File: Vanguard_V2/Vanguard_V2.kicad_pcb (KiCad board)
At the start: 4 copper layers, 55.9 x 30.5 mm, 75 parts, among them IC1 ST1L05CPU33R, IC2 MAX-M10S-00B, IC3 ADXL375BCCZ-RL, IC4 ASM330LHHTR, J1 Conn_01x02_Pin, J2 Conn_01x05_Pin, J3 MEM2067-02-180-00-A, J4 Conn_01x04_Pin, J5 Conn_01x02_Pin, J6 Conn_01x02_Pin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

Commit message: V2 Board Ready
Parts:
- removed R10: 10k, Resistor_SMD:R_0402_1005Metric
- C15, C16, C17, C7, C8, IC1, R3, U2: moved to F.Cu
- C19, C23, C31, C32, D3, FB2, FB3, IC2, J7, R11, R6, R7: moved to B.Cu
- J6: value Conn_01x02_Pin -> Screw_Terminal_01x04; footprint Connector_PinHeader_2.54mm:PinHeader_1x02_P2.54mm_Vertical -> TerminalBlock:TerminalBlock_Xinya_XY308-2.54-4P_1x04_P2.54mm_Horizontal
- moved R7 110.0 mm to (141.4, 85.8), turned to 180 degrees
- moved R6 108.8 mm to (139.8, 85.3), turned to -90 degrees
- moved C11 107.6 mm to (127.0, 78.6), turned to 90 degrees
- moved C10 107.0 mm to (126.0, 78.6), turned to 90 degrees
- moved C9 106.0 mm to (125.0, 78.6), turned to 90 degrees
- moved C12 103.8 mm to (130.0, 78.6), turned to 90 degrees
- moved C13 102.8 mm to (129.0, 78.6), turned to 90 degrees
- moved C19 102.3 mm to (138.2, 85.8), turned to 180 degrees
- moved C14 101.9 mm to (128.0, 78.6), turned to 90 degrees
- moved D1 94.2 mm to (124.4, 101.7), turned to 180 degrees
- moved C26 92.9 mm to (151.9, 91.0)
- moved C25 90.9 mm to (149.6, 91.0), turned to 180 degrees
- moved J5 89.9 mm to (134.9, 74.2), turned to 90 degrees
- moved C24 89.4 mm to (146.8, 95.8), turned to 180 degrees
- moved R5 88.6 mm to (110.3, 100.4), turned to -90 degrees
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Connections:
- C24 pad 1: Net-(IC4-VDDIO) -> +3.3V
- C25 pad 1: Net-(IC4-VDDIO) -> +3.3V
- C26 pad 1: Net-(IC4-VDDIO) -> +3.3V
- IC4 pad 5: Net-(IC4-VDDIO) -> +3.3V
- J6 pad 1: GND -> unconnected-(J6-Pin_1-Pad1)
- J6 pad 2: +3.3V -> unconnected-(J6-Pin_2-Pad2)
- U1 pad 2: unconnected-(U1-PE3-Pad2) -> SERVO_5_PWM
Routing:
- net +3.3V: track 1.46 -> 111.1 mm, vias 0 -> 16
- net I2C1_SCL: track 0.00 -> 99.0 mm, vias 0 -> 6
- net I2C1_SDA: track 0.00 -> 89.0 mm, vias 0 -> 7
- net GND: track 5.82 -> 81.5 mm, vias 2 -> 53
- net BOOT0: track 0.00 -> 40.2 mm, vias 0 -> 2
- net USB_DP: track 0.00 -> 40.1 mm, vias 0 -> 2
- net USB_DM: track 0.00 -> 39.9 mm, vias 0 -> 2
- net RST: track 0.00 -> 30.1 mm
- net SPI1_MOSI: track 0.00 -> 23.4 mm, vias 0 -> 2
- net SERVO_5_PWM: track 0.00 -> 21.1 mm, vias 0 -> 1
- net SPI1_SCK: track 0.00 -> 21.1 mm, vias 0 -> 1
- net Net-(C1-Pad1): track 0.00 -> 18.8 mm, vias 0 -> 2
- net SD_CS: track 0.00 -> 18.5 mm, vias 0 -> 1
- net SPI1_MISO: track 0.00 -> 14.6 mm, vias 0 -> 1
- net SERVO_1_PWM: track 0.57 -> 14.5 mm
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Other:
- board text added: "3.3V"
- board text added: "BOOT"
- board text added: "GPS"
- board text added: "RESET"

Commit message: started layout for V2.1
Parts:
- removed C5, C6: 20pF, Capacitor_SMD:C_0402_1005Metric
- removed Y1: LFXTAL078719Cutt, VanguardLib:LFXTAL078719Cutt
- added D4: D_Schottky, Diode_SMD:D_0603_1608Metric, F.Cu at (112.5, 99.8)
- added D5: D_Schottky, Diode_SMD:D_0603_1608Metric, F.Cu at (113.5, 96.8)
- added Q1: SI7232DN-T1-GE3, VanguardLib:SI7232DNT1GE3, F.Cu at (117.7, 88.5)
- added R10: 10, Resistor_SMD:R_0402_1005Metric, F.Cu at (69.1, 85.4)
- added R12: 10, Resistor_SMD:R_0402_1005Metric, F.Cu at (69.1, 87.4)
- added R13: 10k, Resistor_SMD:R_0402_1005Metric, F.Cu at (69.1, 89.4)
- added R14: 10k, Resistor_SMD:R_0402_1005Metric, F.Cu at (69.1, 91.4)
- added X1: ECS-2520MV-xxx-xx, Oscillator:Oscillator_SMD_ECS_2520MV-xxx-xx-4Pin_2.5x2.0mm, F.Cu at (72.2, 46.6)
- C15, C16, C17, D2, IC1, R3: moved to B.Cu
- C19, C23, C31, C32, FB3, J9, R6, R7: moved to F.Cu
- R11: footprint Capacitor_SMD:C_0402_1005Metric -> Resistor_SMD:R_0402_1005Metric
- moved J6 143.6 mm to (107.3, 101.3), turned to 90 degrees
- moved IC4 119.4 mm to (31.9, 82.1)
- moved IC3 118.5 mm to (25.2, 83.5), turned to 0 degrees
- moved R9 117.2 mm to (33.7, 63.1), turned to 0 degrees
- moved R8 117.2 mm to (33.7, 61.1), turned to 0 degrees
- moved C26 113.8 mm to (40.7, 67.0)
- moved C25 112.7 mm to (37.9, 76.9), turned to 0 degrees
- moved R7 110.9 mm to (33.7, 59.1), turned to 0 degrees
- moved C24 110.9 mm to (37.9, 74.9), turned to 0 degrees
- moved R6 109.7 mm to (33.7, 57.1), turned to 0 degrees
- moved C20 106.1 mm to (37.9, 67.0)
- moved C21 105.4 mm to (37.9, 69.0), turned to 0 degrees
- moved C22 103.6 mm to (37.9, 71.0), turned to 0 degrees
- moved C28 100.0 mm to (40.7, 71.0)
- moved C27 99.3 mm to (40.7, 69.0), turned to 0 degrees
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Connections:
- C7 pad 1: VIN -> C1_P
- J1 pad 1: VIN -> C1_P
- J6 pad 1: unconnected-(J6-Pin_1-Pad1) -> C2_M
- J6 pad 2: unconnected-(J6-Pin_2-Pad2) -> C1_P
- J6 pad 3: unconnected-(J6-Pin_3-Pad3) -> C1_M
- J6 pad 4: unconnected-(J6-Pin_4-Pad4) -> C1_P
- U1 pad 12: OSC_IN -> HSE_BYPASS
- U1 pad 13: OSC_OUT -> unconnected-(U1-PH1-Pad13)
- U1 pad 8: OSC32_IN -> unconnected-(U1-PC14-Pad8)
- U1 pad 9: OSC32_OUT -> unconnected-(U1-PC15-Pad9)
- U2 pad 3: VIN -> C1_P
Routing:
- net +3.3V: track 111.1 -> 15.4 mm, vias 16 -> 2
- net I2C1_SCL: track 99.0 -> 9.73 mm, vias 6 -> 1
- net GND: track 81.5 -> 11.9 mm, vias 53 -> 2
- net I2C1_SDA: track 89.0 -> 25.1 mm, vias 7 -> 1
- net BOOT0: track 40.2 -> 0.00 mm, vias 2 -> 0
- net USB_DP: track 40.1 -> 3.53 mm, vias 2 -> 0
- net USB_DM: track 39.9 -> 3.77 mm, vias 2 -> 0
- net RST: track 30.1 -> 0.00 mm
- net SPI1_MOSI: track 23.4 -> 0.00 mm, vias 2 -> 0
- net SERVO_5_PWM: track 21.1 -> 0.00 mm, vias 1 -> 0
- net SPI1_SCK: track 21.1 -> 0.00 mm, vias 1 -> 0
- net Net-(C1-Pad1): track 18.8 -> 0.00 mm, vias 2 -> 0
- net SD_CS: track 18.5 -> 0.00 mm, vias 1 -> 0
- net +5V: track 19.7 -> 2.24 mm
- net C1_P: track 0.00 -> 17.3 mm
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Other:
- board text removed: "3.3V"
- board text removed: "BOOT"
- board text removed: "GPS"
- board text removed: "RESET"

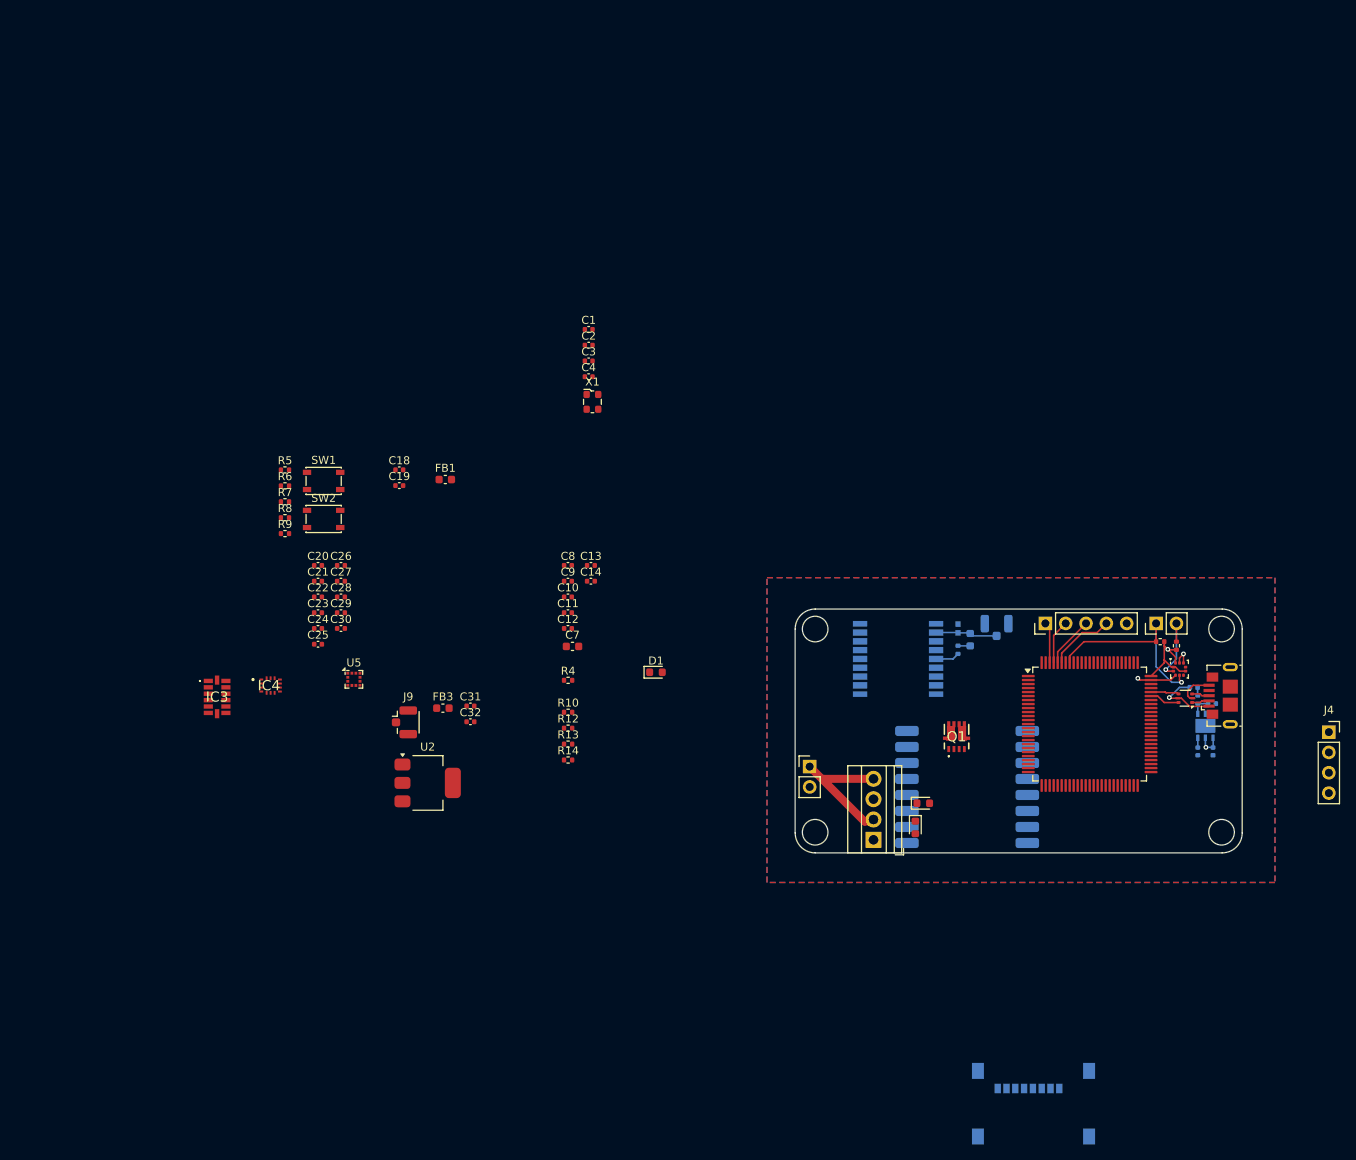
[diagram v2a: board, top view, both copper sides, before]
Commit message: Begun board routing
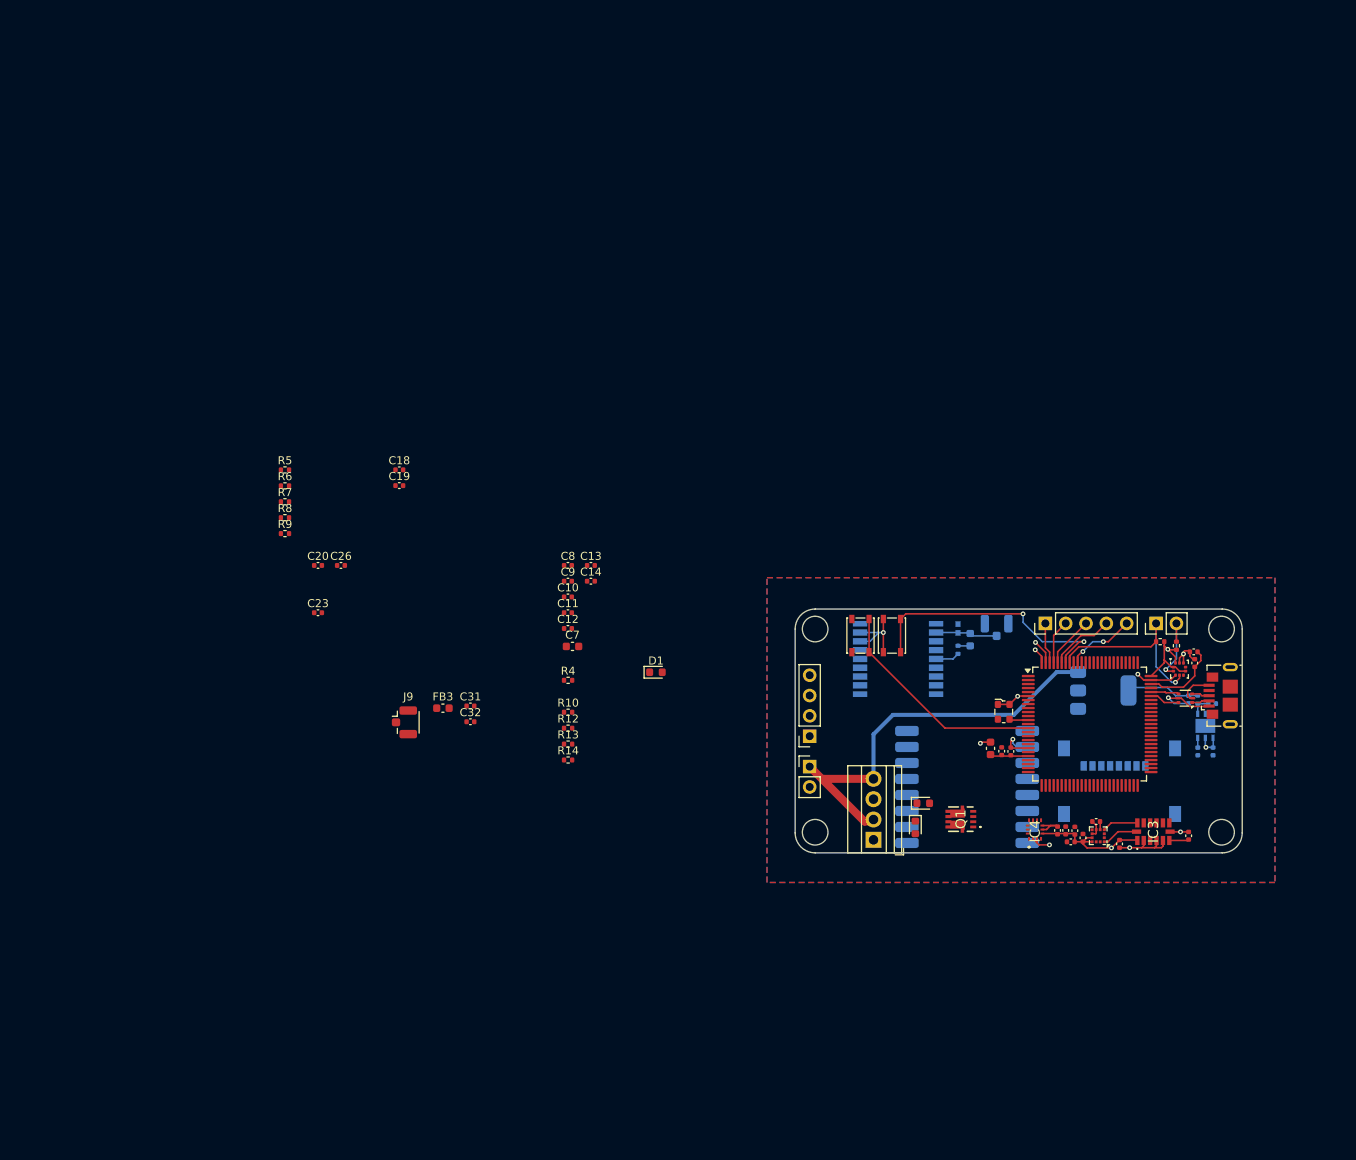
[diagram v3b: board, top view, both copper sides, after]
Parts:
- U2: moved to B.Cu
- moved IC3 118.2 mm to (142.3, 100.3), turned to 90 degrees
- moved C22 112.8 mm to (146.7, 100.8), turned to 90 degrees
- moved C21 105.4 mm to (138.0, 101.9), turned to -90 degrees
- moved C28 98.5 mm to (135.1, 99.1), turned to 180 degrees
- moved IC4 97.2 mm to (127.5, 100.1), turned to 90 degrees
- moved C27 96.9 mm to (132.5, 100.2), turned to 90 degrees
- moved C24 96.8 mm to (131.3, 100.2), turned to 90 degrees
- moved C30 96.4 mm to (133.5, 101.1), turned to 90 degrees
- moved C29 95.6 mm to (132.0, 101.6), turned to 180 degrees
- moved C25 95.3 mm to (130.3, 100.2), turned to 90 degrees
- moved U5 95.1 mm to (135.4, 100.8), turned to 180 degrees
- moved C1 85.7 mm to (147.3, 77.9), turned to 180 degrees
- moved C2 85.5 mm to (147.4, 79.2), turned to 90 degrees
- moved U2 85.2 mm to (136.0, 82.7)
- moved FB1 76.0 mm to (121.9, 89.9), turned to -90 degrees
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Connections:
- Q1 pad 2: Net-(Q1-G1) -> C1_GATE
- Q1 pad 4: Net-(Q1-G2) -> C2_GATE
- U1 pad 2: SERVO_5_PWM -> unconnected-(U1-PE3-Pad2)
- U1 pad 91: unconnected-(U1-PB5-Pad91) -> SERVO_5_PWM
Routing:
- net +3.3V: track 15.4 -> 51.5 mm, vias 2 -> 8
- net C1_P: track 17.3 -> 51.7 mm
- net BOOT0: track 0.00 -> 33.3 mm, vias 0 -> 2
- net GND: track 11.9 -> 40.7 mm, vias 2 -> 6
- net RST: track 0.00 -> 28.0 mm
- net Net-(C1-Pad1): track 0.00 -> 9.69 mm
- net SERVO_5_PWM: track 0.00 -> 8.65 mm, vias 0 -> 2
- net +5V: track 2.24 -> 10.5 mm
- net Net-(U1-VDDA): track 0.00 -> 4.79 mm
- net I2C1_SCL: track 9.73 -> 14.3 mm
- net I2C1_SDA: track 25.1 -> 28.9 mm
- net Net-(IC3-VS): track 0.00 -> 2.46 mm
- net HSE_BYPASS: track 0.00 -> 2.38 mm
- net Net-(U5-C1): track 0.00 -> 1.03 mm

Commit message: Everything is placed
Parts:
- removed R10, R12: 10, Resistor_SMD:R_0402_1005Metric
- C23, C31, C32, C7, C8, FB3, J9: moved to B.Cu
- moved C20 105.8 mm to (143.1, 78.3), turned to 180 degrees
- moved R6 105.3 mm to (131.4, 96.5), turned to 180 degrees
- moved C19 100.7 mm to (140.8, 96.2)
- moved R7 99.6 mm to (126.4, 95.5)
- moved C26 95.5 mm to (130.3, 100.2), turned to 90 degrees
- moved C23 83.8 mm to (121.5, 77.4)
- moved R5 81.4 mm to (112.8, 74.3), turned to -90 degrees
- moved FB3 73.8 mm to (127.3, 85.6)
- moved C8 73.8 mm to (141.4, 81.8), turned to 90 degrees
- moved J9 73.1 mm to (121.7, 83.9), turned to 180 degrees
- moved C31 72.7 mm to (128.8, 95.3), turned to 90 degrees
- moved R9 71.7 mm to (102.2, 84.2), turned to 180 degrees
- moved R8 71.3 mm to (101.8, 82.2), turned to -90 degrees
- moved C32 71.2 mm to (128.1, 83.9), turned to 90 degrees
- moved C18 64.0 mm to (107.2, 79.4), turned to 180 degrees
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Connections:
- J6 pad 1: C2_M -> C1_M
- J6 pad 3: C1_M -> C2_M
- Q1 pad 10: unconnected-(Q1-D1_4-Pad10) -> C1_M
- Q1 pad 11: unconnected-(Q1-D1_5-Pad11) -> C1_M
- Q1 pad 12: unconnected-(Q1-D2_3-Pad12) -> C2_M
- Q1 pad 13: unconnected-(Q1-D2_4-Pad13) -> C2_M
- Q1 pad 14: unconnected-(Q1-D2_5-Pad14) -> C2_M
- Q1 pad 6: unconnected-(Q1-D2_2-Pad6) -> C2_M
- Q1 pad 8: unconnected-(Q1-D1_2-Pad8) -> C1_M
- Q1 pad 9: unconnected-(Q1-D1_3-Pad9) -> C1_M
- U1 pad 15: unconnected-(U1-PC0-Pad15) -> C2_GATE
- U1 pad 24: unconnected-(U1-PA2-Pad24) -> C1_GATE
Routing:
- net I2C1_SCL: track 14.3 -> 91.6 mm, vias 1 -> 5
- net I2C1_SDA: track 28.9 -> 101.3 mm, vias 1 -> 7
- net SWDIO: track 0.00 -> 46.1 mm, vias 0 -> 2
- net SWCLK: track 0.00 -> 43.8 mm, vias 0 -> 4
- net SPI1_MOSI: track 0.00 -> 32.7 mm, vias 0 -> 2
- net SPI1_SCK: track 0.00 -> 31.2 mm, vias 0 -> 2
- net SPI1_MISO: track 0.00 -> 29.3 mm, vias 0 -> 2
- net +3.3V: track 51.5 -> 77.7 mm, vias 8 -> 14
- net SD_CS: track 0.00 -> 19.0 mm, vias 0 -> 1
- net TELEM_CS: track 0.00 -> 16.1 mm, vias 0 -> 1
- net C1_GATE: track 0.00 -> 12.5 mm
- net C2_GATE: track 0.00 -> 12.3 mm
- net C1_M: track 0.00 -> 10.1 mm
- net GND: track 40.7 -> 48.5 mm, vias 6 -> 26
- net C2_M: track 0.00 -> 7.00 mm
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
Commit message: Removed locks
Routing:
- net GND: vias 26 -> 27
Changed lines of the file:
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@@
 			(at -0.209 0 90)
 			(layer "F.SilkS")
+			(hide yes)
 			(effects
 				(font
@@
 			(at 0 0 90)
 			(layer "F.SilkS")
+			(hide yes)
 			(effects
 				(font
@@
 			(at 0 0 90)
 			(layer "F.SilkS")
+			(hide yes)
 			(effects
 				(font
@@
 	)
 	(via
+		(at 141.4 78.3)
+		(size 0.6)
+		(drill 0.3)
+		(layers "F.Cu" "B.Cu")
+		(free yes)
+		(net 2)
+	)
+	(via
 		(at 129.286 101.981)
 		(size 0.6)
@@
 	(segment
 		(start 101.3 92.197)
-		(end 101.3 90.1)
+		(end 104.683 92.197)
 		(width 0.5)
 		(layer "F.Cu")
@@
 	)
 	(segment
-		(start 101.3 92.197)
-		(end 104.683 92.197)
+		(start 102.1 89.3)
+		(end 104.4 87)
 		(width 0.5)
 		(layer "F.Cu")
@@
 	)
 	(segment
+		(start 102.1 92.197)
+		(end 102.1 89.3)
+		(width 0.5)
+		(layer "F.Cu")
+		(net 4)
+	)
+	(segment
 		(start 104.683 92.197)
 		(end 104.8 92.08)
@@
 		(width 0.5)
 		(layer "F.Cu")
-		(net 4)
-	)
-	(segment
-		(start 101.3 90.1)
-		(end 104.4 87)
-		(width 0.5)
-		(layer "F.Cu")
